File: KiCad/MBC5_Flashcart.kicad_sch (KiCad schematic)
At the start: 14 parts, among them J0 CartBus, SW1 SW_SP3T, U1 MBC5, U2 MBM29F033C, U3 FM18W08, U4 74LVC1G332GW,125

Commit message: Release V3
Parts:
- added D1: D, Diode_SMD:D_SOD-123, symbol Device:D
- added M1: Motor_DC, Custom:ANDA-T1035, symbol Motor:Motor_DC
- added Q1: BC817-40,215, Package_TO_SOT_SMD:SOT-23, symbol Device:Q_NPN_BEC
- added R2: 30K, Resistor_SMD:R_0603_1608Metric, symbol Device:R
- added R3: 15Ω, Resistor_SMD:R_0603_1608Metric, symbol Device:R
- added R4: 22Ω, Resistor_SMD:R_0603_1608Metric, symbol Device:R
- J0: footprint Connector_GameBoy:GameBoy_GamePak_CGB-002_P1.50mm_Edge -> HDR_Gameboy_Cartridges:GB_Cartridge
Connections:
- net +5V: now also R3.2
- net GND: now also Q1.2 (E), R4.1
- net Rumble: now reaches U1.26 (AA16)
- net Rumble: now also R2.1
- new net: D1.1 (K), M1.1 (+), R3.1, R4.2
- new net: D1.2 (A), M1.2 (-), Q1.3 (C)
- new net: Q1.1 (B), R2.2
- no-connect marks 5 -> 4

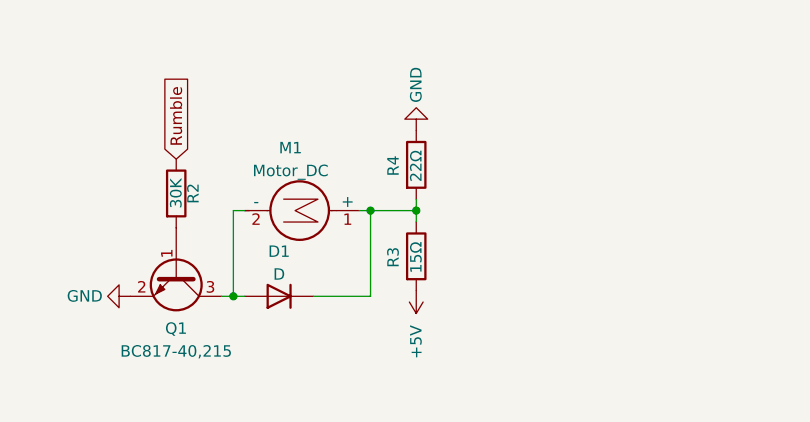
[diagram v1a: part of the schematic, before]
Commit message: Remove R4
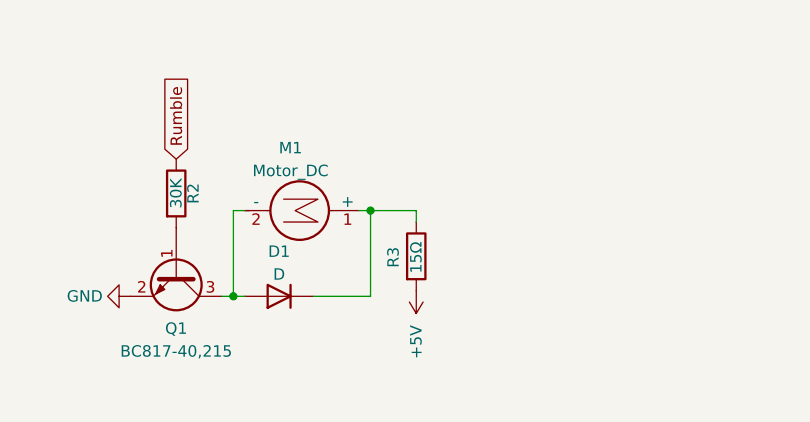
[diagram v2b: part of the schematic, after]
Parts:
- removed R4: 22Ω, Resistor_SMD:R_0603_1608Metric, symbol Device:R
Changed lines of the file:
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@@
 (kicad_sch (version 20211123) (generator eeschema)
   (paper "A4")
-  (junction (at 192.405 45.085) (diameter 0) (color 0 0 0 0)
-  )
   (junction (at 187.325 45.085) (diameter 0) (color 0 0 0 0)
   )
@@
   )
   (wire (pts (xy 187.325 45.085) (xy 187.325 54.61))
-    (stroke (width 0) (type default) (color 0 0 0 0))
-  )
-  (wire (pts (xy 192.405 45.085) (xy 192.405 43.815))
     (stroke (width 0) (type default) (color 0 0 0 0))
   )
@@
     (pin "2")
   )
-  (symbol (lib_id "power:GND") (at 192.405 36.195 180) (unit 1)
-    (in_bom yes) (on_board yes)
-    (property "Reference" "#PWR0129" (id 0) (at 192.405 29.845 0)
-      (effects (font (size 1.27 1.27)) hide)
-    )
-    (property "Value" "GND" (id 1) (at 192.405 31.115 90))
-    (property "Footprint" "" (id 2) (at 192.405 36.195 0)
-      (effects (font (size 1.27 1.27)) hide)
-    )
-    (property "Datasheet" "" (id 3) (at 192.405 36.195 0)
-      (effects (font (size 1.27 1.27)) hide)
-    )
-    (pin "1")
-  )
   (symbol (lib_id "power:GND") (at 222.25 125.095 0) (unit 1)
     (in_bom yes) (on_board yes) (fields_autoplaced)
@@
     )
     (property "Datasheet" "~" (id 3) (at 195.58 99.06 0)
-      (effects (font (size 1.27 1.27)) hide)
-    )
-    (pin "1")
-    (pin "2")
-  )
-  (symbol (lib_id "Device:R") (at 192.405 40.005 0) (unit 1)
-    (in_bom yes) (on_board yes)
-    (property "Reference" "R4" (id 0) (at 189.865 41.275 90)
-      (effects (font (size 1.27 1.27)) (justify left))
-    )
-    (property "Value" "22Ω" (id 1) (at 192.405 41.91 90)
-      (effects (font (size 1.27 1.27)) (justify left))
-    )
-    (property "Footprint" "Resistor_SMD:R_0603_1608Metric" (id 2) (at 190.627 40.005 90)
-      (effects (font (size 1.27 1.27)) hide)
-    )
-    (property "Datasheet" "~" (id 3) (at 192.405 40.005 0)
       (effects (font (size 1.27 1.27)) hide)
     )
@@
       (reference "#PWR0128") (unit 1) (value "GND") (footprint "")
     )
-    (path "/4c56c2b6-966a-460b-9fae-2fcea7646c10"
-      (reference "#PWR0129") (unit 1) (value "GND") (footprint "")
-    )
     (path "/53861fec-ebf8-4c44-bbec-42421127ae6d"
       (reference "#PWR0130") (unit 1) (value "+5V") (footprint "")
@@
       (reference "R3") (unit 1) (value "15Ω") (footprint "Resistor_SMD:R_0603_1608Metric")
     )
-    (path "/592daab7-8c24-43b7-ad5e-b6998fb3c527"
-      (reference "R4") (unit 1) (value "22Ω") (footprint "Resistor_SMD:R_0603_1608Metric")
-    )
     (path "/a2ab2b8e-de65-4bf8-a643-15355633be98"
